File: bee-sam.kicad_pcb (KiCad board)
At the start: 2 copper layers, 29 x 53.3 mm, 30 parts, among them J1 Conn_01x02_Male, J2 Conn_01x02_Male, J3 Conn_01x02_Male, J4 Conn_01x02_Male, J6 Screw_Terminal_01x02, J7 Conn_01x02, J8 Conn_01x02, U2 LM380N

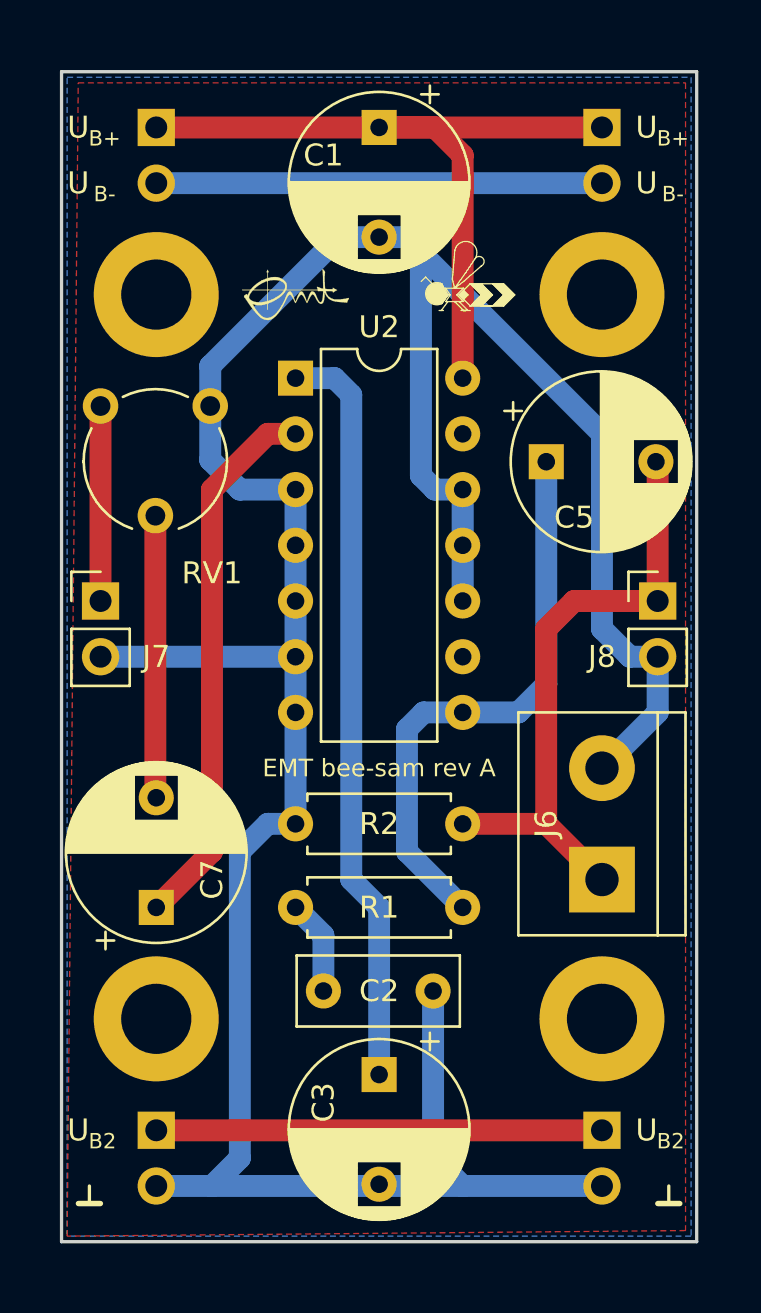
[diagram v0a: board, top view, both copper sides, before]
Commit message: Refactoring
* Replace capacitor footprints with more versatile footprints
* Print device values on pcb
* Adapt spacings between components and heatsink
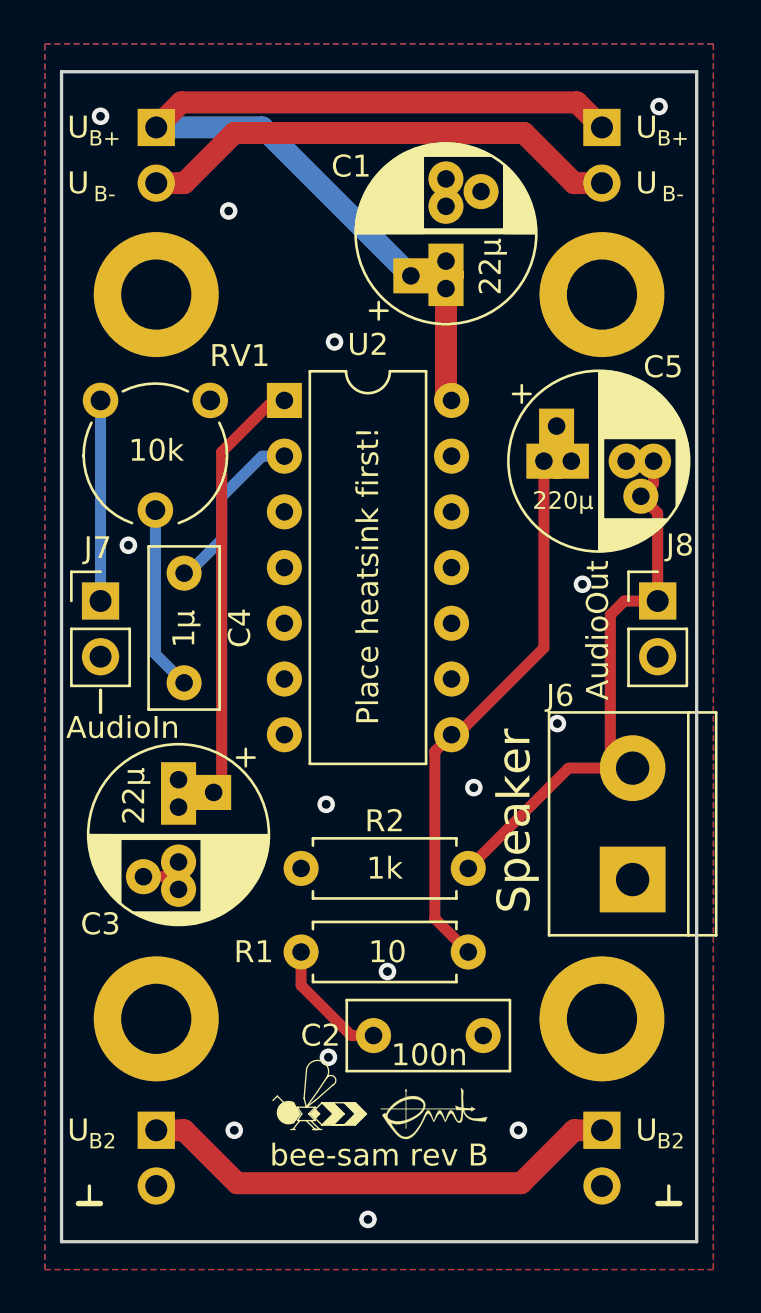
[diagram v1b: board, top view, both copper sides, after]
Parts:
- removed C7: 1 µF, Capacitor_THT:CP_Radial_D8.0mm_P5.00mm
- added C4: 1µ, Capacitor_THT:C_Rect_L7.2mm_W3.0mm_P5.00mm_FKS2_FKP2_MKS2_MKP2, F.Cu at (80.0, 111.8)
- added H15: Silkscreen_Label, Symbol-emt:EMT-Logo_8.2x4.1mm_Silkscreen, B.Cu at (88.4, 137.1)
- C1, C3: value 220 µF -> 22µ; footprint Capacitor_THT:CP_Radial_D8.0mm_P5.00mm -> kicad-footprints-bee:CP_Radial_D8.0mm_P2.50mm_P3.80mm_P5.00mm
- C2: value C -> 100n
- C5: value 220 µF -> 220µ; footprint Capacitor_THT:CP_Radial_D8.0mm_P5.00mm -> kicad-footprints-bee:CP_Radial_D8.0mm_P2.50mm_P3.80mm_P5.00mm
- J6: value Screw_Terminal_01x02 -> Speaker
- J7: value Conn_01x02 -> AudioIn
- J8: value Conn_01x02 -> AudioOut
- R1: value 10R -> 10
- RV1: value R_POT -> 10k
- moved H14 37.9 mm to (86.0, 136.4)
- moved H13 37.9 mm to (91.4, 136.4)
- moved C3 15.2 mm to (79.8, 122.4)
- moved C1 6.82 mm to (91.9, 97.5), turned to 90 degrees
- moved C2 3.06 mm to (88.6, 132.8)
- moved R1 2.05 mm to (93.0, 129.0)
- moved R2 2.05 mm to (93.0, 125.2)
- moved J6 1.40 mm to (100.5, 125.7)
- moved C5 1.14 mm to (97.7, 106.7)
- moved U2 1.14 mm to (84.6, 103.9)
- moved RV1 0.25 mm to (76.2, 103.9)
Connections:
- J6 pad 1: Net-(C5-Pad2) -> GND
- J6 pad 2: GND -> Net-(C5-Pad2)
- U2 pad 13: (no net) -> Net-(U2-Pad13)
- U2 pad 9: (no net) -> Net-(U2-Pad9)
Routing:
- net GND: track 143.6 -> 3.09 mm, vias 0 -> 14
- net Net-(C4-Pad1): track 25.0 -> 7.93 mm
- net Net-(C3-Pad1): track 34.4 -> 24.5 mm
- net +15V: track 34.8 -> 44.0 mm
- net Net-(C4-Pad2): track 12.9 -> 8.42 mm
- net +5V: track 20.3 -> 22.3 mm
- net -15V: track 20.3 -> 22.2 mm
- net Net-(C2-Pad1): track 4.34 -> 5.77 mm
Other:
- net class Default: trace_width 0.25 -> 0.5
- net class Supply added: clearance 0.2, trace_width 1, via_dia 1, via_drill 0.7
- board text added: "Place heatsink first!"
- board text added: "Speaker"
- board text added: "bee-sam rev B"
- board text removed: "EMT bee-sam rev A"
